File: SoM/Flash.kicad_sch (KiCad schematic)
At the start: 17 parts, among them U2 MX25V8035F

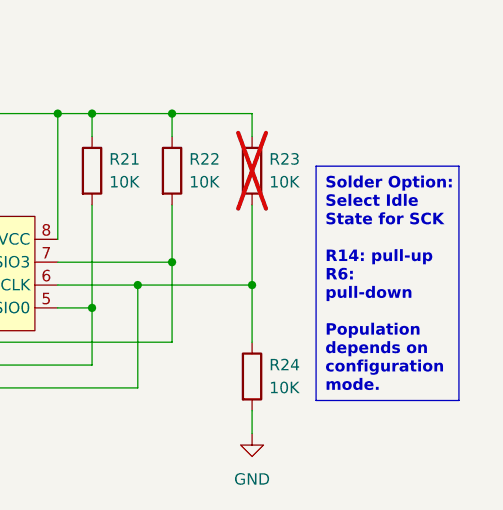
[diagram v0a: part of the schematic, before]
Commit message: Created Version with 0402 components
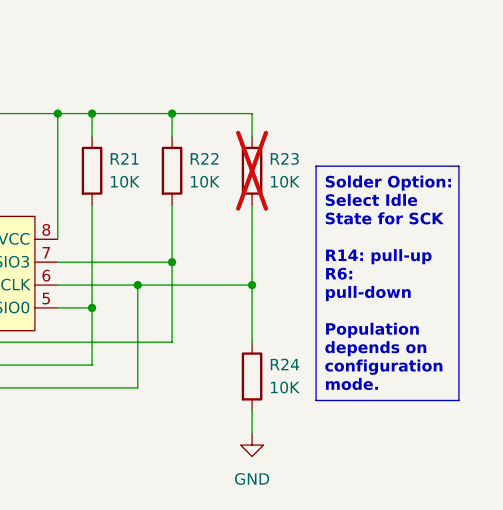
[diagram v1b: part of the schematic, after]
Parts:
- C41: footprint Capacitor_SMD:C_0201_0603Metric -> Capacitor_SMD:C_0402_1005Metric; Mouser Part Number 187-CL03A225KP3CRNC -> GRM155Z71A225KE44D; Part Number (none) -> GRM155Z71A225KE44D
- C42, C43: footprint Capacitor_SMD:C_0201_0603Metric -> Capacitor_SMD:C_0402_1005Metric; Mouser Part Number 187-CL03A104KP3NNNC -> GRM155R71C104KA88J; Part Number (none) -> GRM155R71C104KA88J
- R18, R19, R20, R22, R24: footprint Resistor_SMD:R_0201_0603Metric -> Resistor_SMD:R_0402_1005Metric; Mouser Part Number 71-CRCW0201-10K -> MCS0402MC1002FE000; Part Number (none) -> MCS0402MC1002FE000
- R21: footprint Resistor_SMD:R_0201_0603Metric -> Resistor_SMD:R_0402_1005Metric; Mouser Part Number (none) -> MCS0402MC1002FE000; Part Number (none) -> MCS0402MC1002FE000
- R23: footprint Resistor_SMD:R_0201_0603Metric -> Resistor_SMD:R_0402_1005Metric
- U2: Mouser Part Number 95-25V8035FM1ITR -> MX25V8035FM2I; Part Number (none) -> MX25V8035FM2I
